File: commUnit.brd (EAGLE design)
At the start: 13 parts

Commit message: dokreslen DPS
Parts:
- removed JP1, JP2: (no value), pinhead:1X02
- removed JP3, JP4: (no value), pinhead:1X06
- removed UART: (no value), con-wago-508:W237-133
- added NAP33: (no value), con-wago-508:W237-132
- added UART1: (no value), con-wago-508:W237-133
- moved LED2 150.2 mm to (17.8, 35.6)
- moved R2 137.8 mm to (19.1, 19.1), turned to 90 degrees
- moved UART2 133.8 mm to (26.7, 6.35)
- moved U$2 118.2 mm to (24.1, 14.0)
- moved C1 83.9 mm to (22.9, 43.2), turned to 90 degrees
- moved LED1 63.9 mm to (17.8, 27.9)
- moved R1 51.2 mm to (16.5, 19.1), turned to 90 degrees
- moved U$1 36.9 mm to (3.81, 14.0)
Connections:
- removed net +5V: JP2.2, JP4.6
- removed net N$10: JP4.3, UART2.3
- removed net N$3: JP3.3, U$1.P$5
- net +3V3: now also NAP33.2; no longer JP1.1, JP3.1
- net GND: now also NAP33.1, UART1.1; no longer JP1.2, JP2.1, JP3.2, JP4.5, UART.1
- net N$4: now also UART1.2; no longer UART.2
- net N$5: now also U$1.P$5, UART1.3; no longer JP4.4, UART.3
- net N$9: now also UART2.3; no longer JP3.4
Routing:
- net GND: track 0.00 -> 137.8 mm
- net +3V3: track 0.00 -> 81.6 mm
- net N$2: track 0.00 -> 29.2 mm
- net N$7: track 0.00 -> 26.7 mm
- net N$6: track 0.00 -> 19.1 mm
- net N$9: track 0.00 -> 14.6 mm
- net N$5: track 0.00 -> 13.3 mm
- net N$4: track 0.00 -> 13.3 mm
- net N$8: track 0.00 -> 10.8 mm
- net N$1: track 0.00 -> 3.81 mm
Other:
- board outline added: 36.8 x 48.9 mm

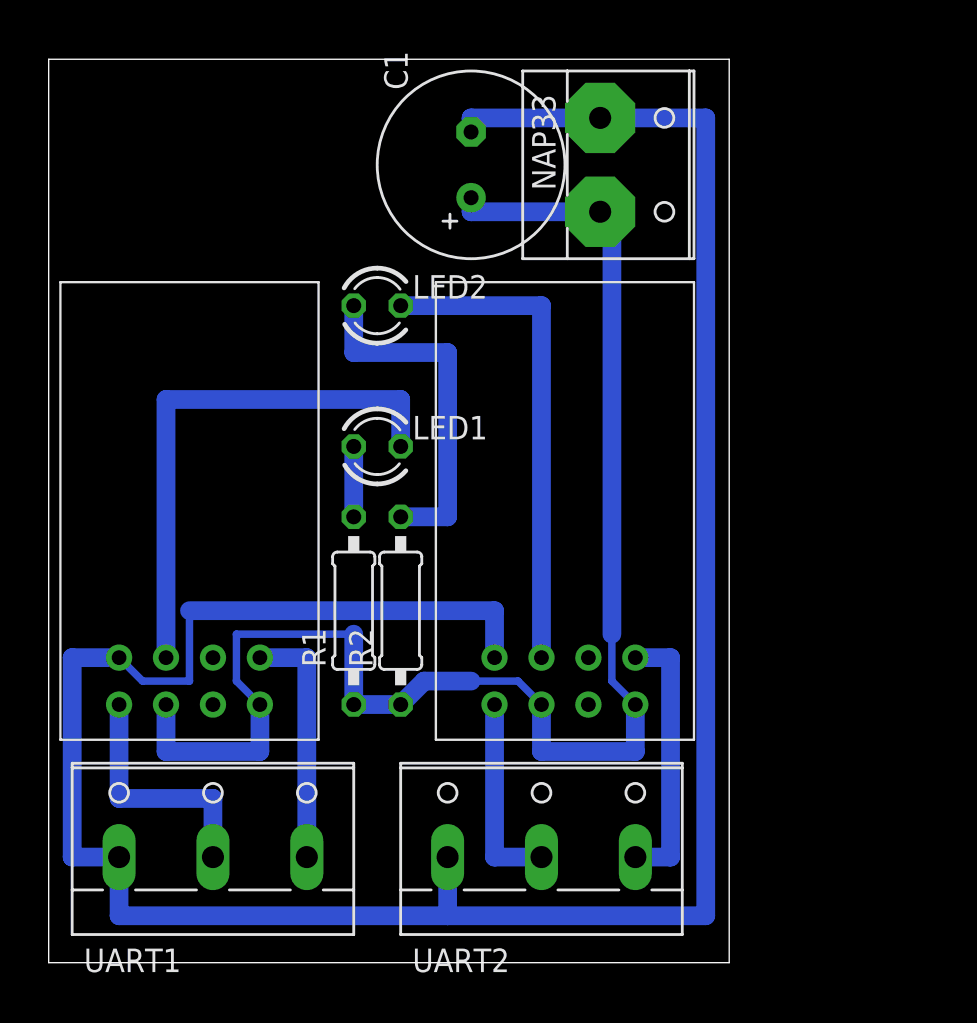
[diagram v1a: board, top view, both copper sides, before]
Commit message: +upraveny DPS DPS objednany 27.4.2016
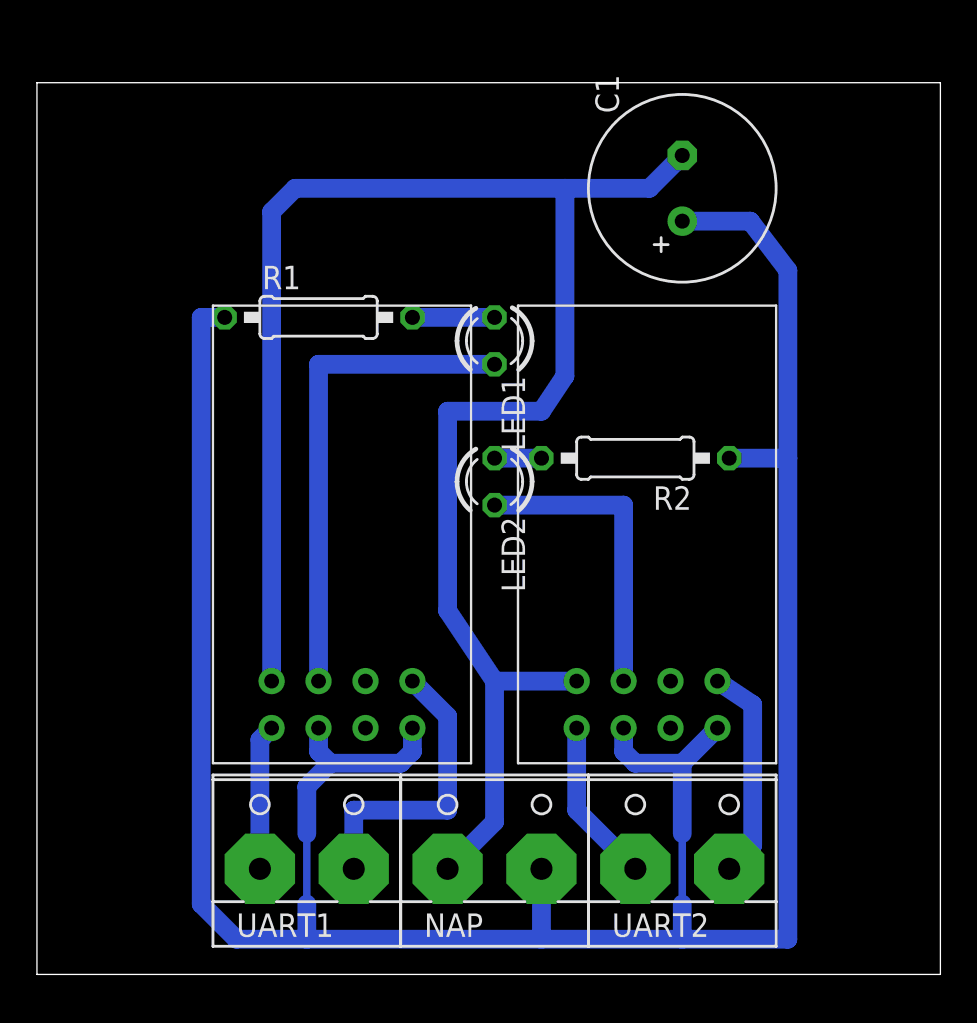
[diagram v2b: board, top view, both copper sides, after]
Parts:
- removed NAP33: (no value), con-wago-508:W237-132
- added NAP: (no value), con-wago-508:W237-132
- UART1, UART2: device con-wago-508:W237-133 -> con-wago-508:W237-132
- moved R1 16.0 mm to (14.6, 34.9), turned to 0 degrees
- moved R2 15.1 mm to (31.8, 27.3), turned to 180 degrees
- moved C1 11.5 mm to (34.3, 41.9)
- moved LED2 11.4 mm to (24.1, 26.0), turned to 270 degrees
- moved LED1 8.54 mm to (24.1, 33.7), turned to 270 degrees
- moved U$1 8.35 mm to (12.1, 12.7)
- moved UART2 7.65 mm to (34.3, 5.71)
- moved UART1 5.12 mm to (14.0, 5.71)
- moved U$2 4.62 mm to (28.6, 12.7)
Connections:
- removed net N$9: U$2.P$5, UART2.3
- new net N$3: U$1.P$5, UART1.2
- net +3V3: now also NAP.2; no longer NAP33.2
- net GND: now also NAP.1; no longer NAP33.1, UART1.1, UART2.1
- net N$4: now also UART1.1; no longer UART1.2
- net N$5: now also U$2.P$5, UART2.2; no longer U$1.P$5, UART1.3
- net N$8: now also UART2.1; no longer UART2.2
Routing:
- net +3V3: track 81.6 -> 150.9 mm
- net GND: track 137.8 -> 97.4 mm
- net N$6: track 19.1 -> 2.54 mm
- net N$3: track 0.00 -> 16.0 mm
- net N$9: track 14.6 -> 0.00 mm
- net N$7: track 26.7 -> 16.5 mm
- net N$4: track 13.3 -> 7.88 mm
- net N$2: track 29.2 -> 26.7 mm
- net N$8: track 10.8 -> 8.94 mm
- net N$5: track 13.3 -> 11.7 mm
- net N$1: track 3.81 -> 4.45 mm
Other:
- board size 36.8 x 48.9 mm -> 48.9 x 48.3 mm
